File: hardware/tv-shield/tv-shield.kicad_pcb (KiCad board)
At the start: 2 copper layers, 25.6 x 25.6 mm, 9 parts, among them J1 D1 Mini left row, J2 D1 Mini right row, J3 SJ1-3523N, J4 cable

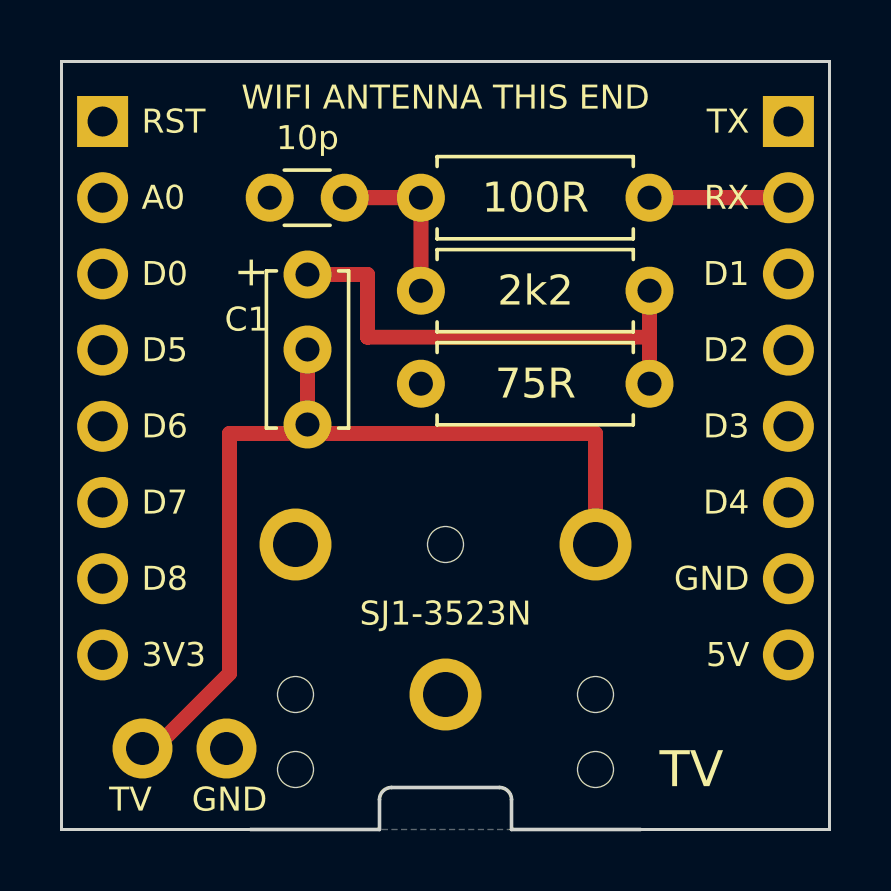
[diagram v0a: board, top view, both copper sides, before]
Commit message: Use a socket from Conrad on the through-hole TV board
The TRU Components TC-9465728 (Conrad item 2366432) replaces the CUI
SJ1-3523N, which is only sold where shipping costs more than the part.
It is drawn from its data sheet and smaller, so the notch in the board
edge is gone. Not tried with a real socket yet.

Co-Authored-By: Claude Opus 5.5 <noreply@anthropic.com>
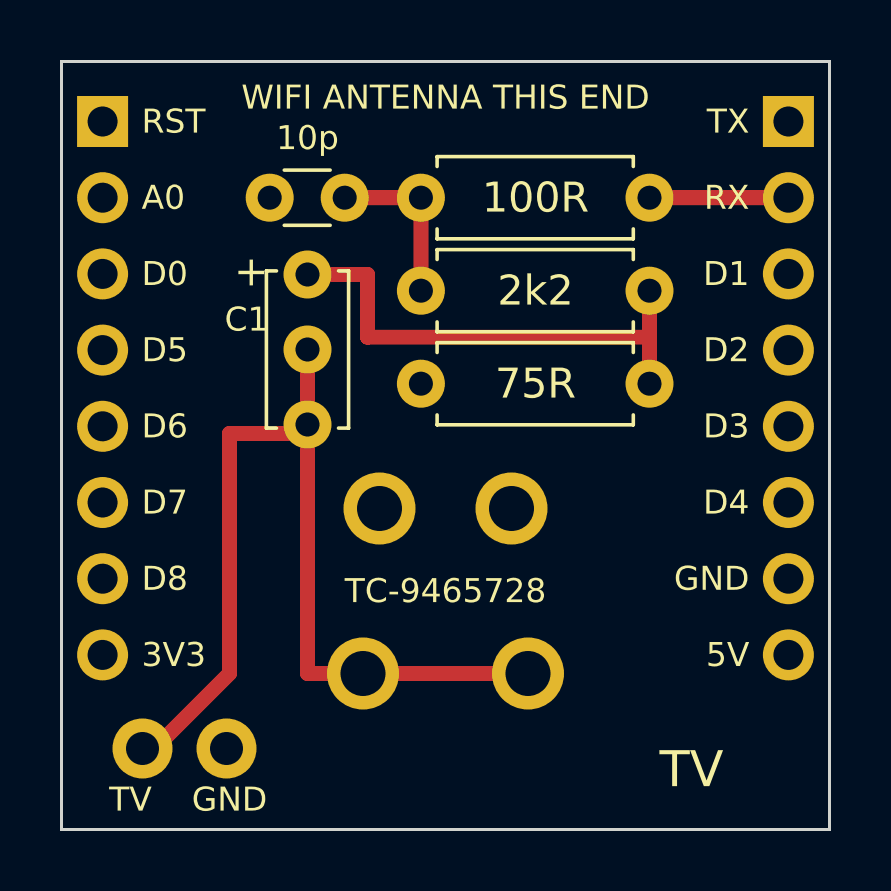
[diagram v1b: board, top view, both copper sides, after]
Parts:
- J3: value SJ1-3523N -> TC-9465728; footprint Jack_3.5mm_CUI_SJ1-3523N_Horizontal -> (none)
- moved J3 3.45 mm to (12.8, 17.6)
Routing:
- net TV: track 30.6 -> 32.7 mm
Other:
- outline, holes or cut-outs redrawn
- board text added: "TC-9465728"
- board text removed: "SJ1-3523N"
